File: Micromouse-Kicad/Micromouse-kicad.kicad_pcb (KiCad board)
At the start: 4 copper layers, 106.4 x 103.1 mm, 99 parts, among them J1 SWD, J2 USB_B_Micro, J3 UARTBTH, J4 Batería, J5 VL6180x, J6 MotorEncodL, J7 MotorEncodR, Q1 BS170, Q2 BS170, Q3 BS170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

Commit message: Cabra
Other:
- board text added: "RAS"

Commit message: Ajuste VL180X
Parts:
- moved J5 15.2 mm to (95.2, 110.5), turned to 180 degrees
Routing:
- net I2C2_SCL: track 72.0 -> 76.3 mm
- net I2C2_SDA: track 75.8 -> 77.2 mm, vias 3 -> 1
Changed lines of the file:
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@@
   )
   (footprint "Connector_PinSocket_2.54mm:PinSocket_1x07_P2.54mm_Vertical" (layer "F.Cu")
-    (at 95.275 95.27)
+    (at 95.25 110.49 180)
     (descr "Through hole straight socket strip, 1x07, 2.54mm pitch, single row (from Kicad 4.0.7), script generated")
     (tags "Through hole socket strip THT 1x07 2.54mm single row")
@@
     (fp_line (start -1.27 16.51) (end -1.27 -1.27) (layer "F.Fab") (width 0.1))
     (fp_line (start 0.635 -1.27) (end 1.27 -0.635) (layer "F.Fab") (width 0.1))
-    (pad "1" thru_hole rect (at 0 0) (size 1.7 1.7) (drill 1) (layers *.Cu *.Mask)
+    (pad "1" thru_hole rect (at 0 0 180) (size 1.7 1.7) (drill 1) (layers *.Cu *.Mask)
       (net 1 "+3.3V") (pinfunction "Pin_1") (pintype "passive"))
-    (pad "2" thru_hole oval (at 0 2.54) (size 1.7 1.7) (drill 1) (layers *.Cu *.Mask)
+    (pad "2" thru_hole oval (at 0 2.54 180) (size 1.7 1.7) (drill 1) (layers *.Cu *.Mask)
       (net 33 "unconnected-(J5-Pad2)") (pinfunction "Pin_2") (pintype "passive+no_connect"))
-    (pad "3" thru_hole oval (at 0 5.08) (size 1.7 1.7) (drill 1) (layers *.Cu *.Mask)
+    (pad "3" thru_hole oval (at 0 5.08 180) (size 1.7 1.7) (drill 1) (layers *.Cu *.Mask)
       (net 2 "GND") (pinfunction "Pin_3") (pintype "passive"))
-    (pad "4" thru_hole oval (at 0 7.62) (size 1.7 1.7) (drill 1) (layers *.Cu *.Mask)
+    (pad "4" thru_hole oval (at 0 7.62 180) (size 1.7 1.7) (drill 1) (layers *.Cu *.Mask)
       (net 34 "unconnected-(J5-Pad4)") (pinfunction "Pin_4") (pintype "passive+no_connect"))
-    (pad "5" thru_hole oval (at 0 10.16) (size 1.7 1.7) (drill 1) (layers *.Cu *.Mask)
+    (pad "5" thru_hole oval (at 0 10.16 180) (size 1.7 1.7) (drill 1) (layers *.Cu *.Mask)
       (net 35 "unconnected-(J5-Pad5)") (pinfunction "Pin_5") (pintype "passive+no_connect"))
-    (pad "6" thru_hole oval (at 0 12.7) (size 1.7 1.7) (drill 1) (layers *.Cu *.Mask)
+    (pad "6" thru_hole oval (at 0 12.7 180) (size 1.7 1.7) (drill 1) (layers *.Cu *.Mask)
       (net 36 "I2C2_SCL") (pinfunction "Pin_6") (pintype "passive"))
-    (pad "7" thru_hole oval (at 0 15.24) (size 1.7 1.7) (drill 1) (layers *.Cu *.Mask)
+    (pad "7" thru_hole oval (at 0 15.24 180) (size 1.7 1.7) (drill 1) (layers *.Cu *.Mask)
       (net 37 "I2C2_SDA") (pinfunction "Pin_7") (pintype "passive"))
     (model "${KICAD6_3DMODEL_DIR}/Connector_PinSocket_2.54mm.3dshapes/PinSocket_1x07_P2.54mm_Vertical.wrl"
@@
       (scale (xyz 1 1 1))
       (rotate (xyz 0 0 0))
+    )
+    (model "C:/Users/Tatan/3D Objects/KicadModels/vl6180x-carrier-model.step"
+      (offset (xyz 2.5 -16.25 12.8))
+      (scale (xyz 1 1 1))
+      (rotate (xyz 0 -90 0))
+    )
+    (model "C:/Users/Tatan/3D Objects/KicadModels/1x7 Male Pin Header Angle.STEP"
+      (offset (xyz 0 0.125 10))
+      (scale (xyz 1 1 1))
+      (rotate (xyz 90 0 -90))
     )
   )
@@
   (gr_line (start 128.778 128.016) (end 139.192 128.016) (layer "Edge.Cuts") (width 0.1))
   (gr_line (start 195.326 52.578) (end 195.326 152.654) (layer "Edge.Cuts") (width 0.1))
-  (gr_text "SDA" (at 98 110.85 90) (layer "F.SilkS")
+  (gr_text "SDA" (at 98.552 94.996 90) (layer "F.SilkS")
     (effects (font (size 1 1) (thickness 0.15)))
   )
@@
     (effects (font (size 1 1) (thickness 0.15)))
   )
-  (gr_text "SCL" (at 98.1 107.45 90) (layer "F.SilkS")
+  (gr_text "SCL" (at 98.552 98.044 90) (layer "F.SilkS")
     (effects (font (size 1 1) (thickness 0.15)))
   )
@@
     (effects (font (size 1 1) (thickness 0.15)))
   )
-  (gr_text "3.3v\n" (at 97.85 94.9 90) (layer "F.SilkS")
+  (gr_text "3.3v\n" (at 98.806 110.744 90) (layer "F.SilkS")
     (effects (font (size 1 1) (thickness 0.15)))
   )
-  (gr_text "GND\n" (at 97.9 100.05 90) (layer "F.SilkS")
+  (gr_text "GND\n" (at 98.806 105.41 90) (layer "F.SilkS")
     (effects (font (size 1 1) (thickness 0.15)))
   )
@@
   (via (at 146.7612 105.6781) (size 0.8) (drill 0.4) (layers "F.Cu" "B.Cu") (net 36))
   (via (at 148.0312 104.3291) (size 0.8) (drill 0.4) (layers "F.Cu" "B.Cu") (net 36))
+  (segment (start 95.25 97.79) (end 97.322733 97.79) (width 0.3) (layer "B.Cu") (net 36))
   (segment (start 142.727761 105.6781) (end 146.7612 105.6781) (width 0.3) (layer "B.Cu") (net 36))
   (segment (start 146.7612 105.6781) (end 148.0312 104.4081) (width 0.15) (layer "B.Cu") (net 36))
-  (segment (start 95.275 107.97) (end 140.435861 107.97) (width 0.3) (layer "B.Cu") (net 36))
   (segment (start 148.0312 104.4081) (end 148.0312 104.3291) (width 0.15) (layer "B.Cu") (net 36))
   (segment (start 140.435861 107.97) (end 142.727761 105.6781) (width 0.3) (layer "B.Cu") (net 36))
+  (segment (start 97.322733 97.79) (end 107.502733 107.97) (width 0.3) (layer "B.Cu") (net 36))
+  (segment (start 107.502733 107.97) (end 140.435861 107.97) (width 0.3) (layer "B.Cu") (net 36))
   (segment (start 157.1264 105.0036) (end 157.8376 105.7148) (width 0.15) (layer "F.Cu") (net 37))
   (segment (start 144.0826 105.0036) (end 149.9964 105.0036) (width 0.15) (layer "F.Cu") (net 37))
@@
   (segment (start 149.9964 105.0036) (end 157.1264 105.0036) (width 0.15) (layer "F.Cu") (net 37))
   (segment (start 157.9324 105.62) (end 159.35 105.62) (width 0.3) (layer "F.Cu") (net 37))
-  (segment (start 114.15 109.1) (end 114.15 107.5) (width 0.3) (layer "F.Cu") (net 37))
   (segment (start 139.75 106.9) (end 148.1 106.9) (width 0.3) (layer "F.Cu") (net 37))
   (segment (start 157.8376 105.7148) (end 157.9324 105.62) (width 0.3) (layer "F.Cu") (net 37))
-  (segment (start 114.15 107.5) (end 116.05 105.6) (width 0.3) (layer "F.Cu") (net 37))
   (segment (start 148.1 106.9) (end 149.9964 105.0036) (width 0.3) (layer "F.Cu") (net 37))
   (via (at 139.75 106.9) (size 0.55) (drill 0.4) (layers "F.Cu" "B.Cu") (net 37))
-  (via (at 116.05 105.6) (size 0.55) (drill 0.4) (layers "F.Cu" "B.Cu") (net 37))
-  (via (at 114.15 109.1) (size 0.55) (drill 0.4) (layers "F.Cu" "B.Cu") (net 37))
   (segment (start 138.45 105.6) (end 139.75 106.9) (width 0.3) (layer "B.Cu") (net 37))
+  (segment (start 105.7 95.25) (end 95.25 95.25) (width 0.3) (layer "B.Cu") (net 37))
   (segment (start 116.05 105.6) (end 138.45 105.6) (width 0.3) (layer "B.Cu") (net 37))
-  (segment (start 95.275 110.51) (end 96.685 109.1) (width 0.3) (layer "B.Cu") (net 37))
-  (segment (start 96.685 109.1) (end 114.15 109.1) (width 0.3) (layer "B.Cu") (net 37))
+  (segment (start 116.05 105.6) (end 105.7 95.25) (width 0.3) (layer "B.Cu") (net 37))
   (segment (start 174.8536 104.5464) (end 174.8536 104.902) (width 0.261112) (layer "F.Cu") (net 38))
   (segment (start 182.178 97.222) (end 174.8536 104.5464) (width 0.261112) (layer "F.Cu") (net 38))

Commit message: arreglo módulo frontal
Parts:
- moved J5 15.9 mm to (100.3, 95.4), turned to 0 degrees
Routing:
- net I2C2_SCL: track 76.3 -> 67.0 mm
- net I2C2_SDA: track 77.2 -> 69.2 mm
- net L_Reciever: track 83.5 -> 82.2 mm
- net /HSE_IN: track 7.44 -> 6.62 mm
- net GND: track 138.1 -> 137.4 mm
- net Net-(R18-Pad1): track 2.24 -> 1.63 mm
- net Net-(R9-Pad1): track 2.31 -> 1.71 mm
- net Net-(R17-Pad1): track 2.11 -> 1.55 mm
- net +3.3V: track 90.2 -> 89.7 mm
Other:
- board size 106.4 x 103.1 mm -> 99.2 x 98.9 mm
- board text removed: "3.3v"
- board text removed: "SCL"
- board text removed: "SDA"

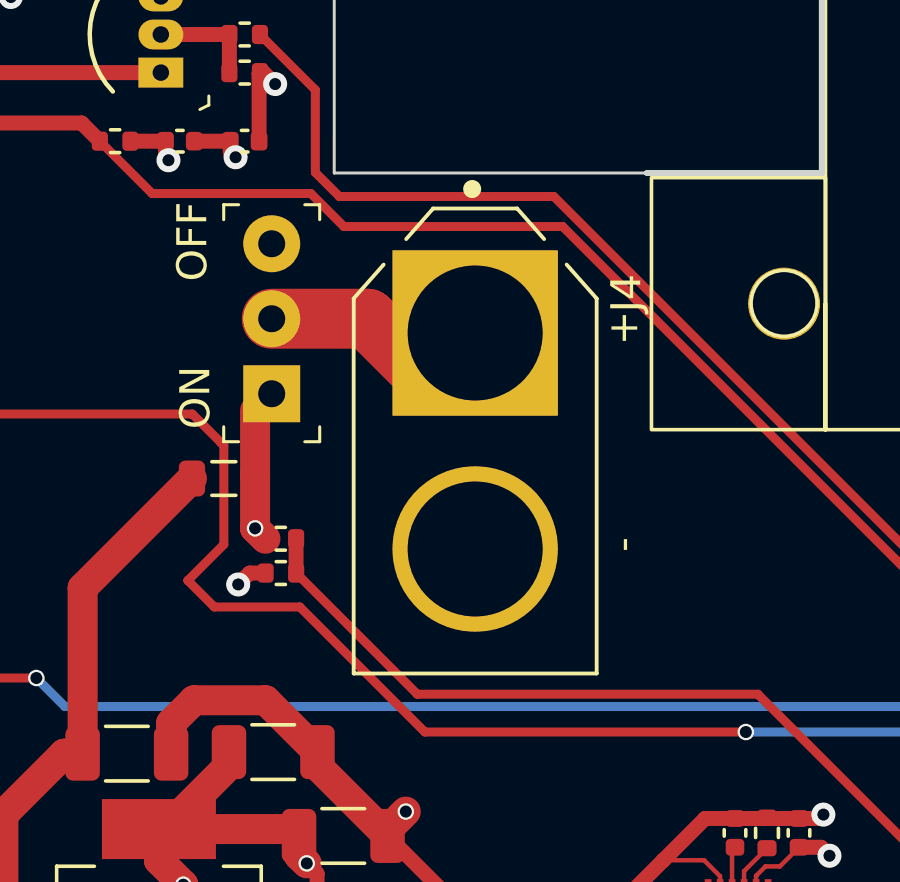
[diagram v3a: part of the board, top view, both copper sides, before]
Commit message: arreglo conector potencia
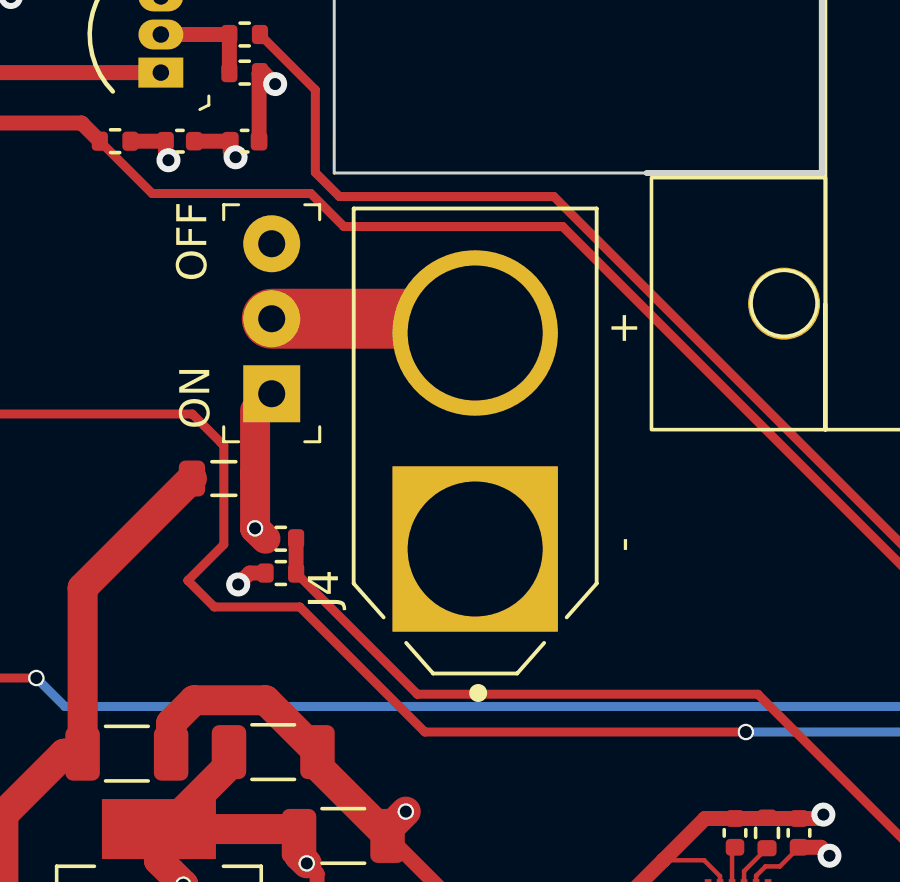
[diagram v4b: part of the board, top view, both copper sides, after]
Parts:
- turned J4 to 90 degrees
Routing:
- net VAA: track 6.07 -> 6.98 mm

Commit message: Arreglos pines stm32
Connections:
- J3 pad 4: UART4_RX -> USART2_RX
- J3 pad 5: UART4_TX -> USART2_TX
- J4 pad 1: GND -> VAA
- J4 pad 2: VAA -> GND
- RU1 pad 2: /USB_STM32_D+ -> DP
- RU2 pad 2: /USB_STM32_D- -> DM
- RU3 pad 2: /USB_STM32_D+ -> DP
- U1 pad 16: FR_Emitter -> USART2_TX
- U1 pad 17: FL_Emitter -> USART2_RX
- U1 pad 20: R_Emitter -> unconnected-(U1-PA4-Pad20)
- U1 pad 21: L_Emitter -> R_Emitter
- U1 pad 22: unconnected-(U1-Pad22) -> L_Emitter
- U1 pad 23: unconnected-(U1-Pad23) -> FR_Emitter
- U1 pad 26: unconnected-(U1-Pad26) -> FL_Emitter
- U1 pad 35: UART4_TX -> DM
- U1 pad 36: UART4_RX -> DP
- U1 pad 52: /USB_STM32_D- -> unconnected-(U1-PC11-Pad52)
- U1 pad 53: /USB_STM32_D+ -> unconnected-(U1-PC12-Pad53)
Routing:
- net (no net): track 0.00 -> 140.3 mm, vias 0 -> 1
- net UART4_RX: track 54.9 -> 0.00 mm, vias 1 -> 0
- net UART4_TX: track 49.9 -> 0.00 mm
- net /USB_STM32_D+: track 18.6 -> 0.00 mm
- net /USB_STM32_D-: track 16.8 -> 0.00 mm

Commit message: Fabricado!
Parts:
- added ?: , , F.Cu at (186.7, 61.8)
- added ?: , , F.Cu at (186.7, 144.7)
- added ?: , , F.Cu at (109.6, 99.8)
- J6, J7: footprint Connector_JST:JST_XH_B6B-XH-A_1x06_P2.50mm_Vertical -> Connector_JST:JST_SH_BM06B-SRSS-TB_1x06-1MP_P1.00mm_Vertical
- moved J5 15.2 mm to (100.3, 110.6), turned to 180 degrees
- moved RU1 13.2 mm to (163.6, 113.2), turned to 90 degrees
- moved J6 6.49 mm to (186.0, 90.4)
- moved J7 6.48 mm to (186.0, 72.2)
- moved DL2 1.67 mm to (166.4, 116.4), turned to 180 degrees
- moved R1 1.11 mm to (165.6, 113.9)
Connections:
- net DM renamed /USB_STM32_D-
- net DP renamed /USB_STM32_D+
- J4 pad 1: VAA -> GND
- J4 pad 2: GND -> VAA
- U1 pad 21: R_Emitter -> L_Emitter
- U1 pad 22: L_Emitter -> R_Emitter
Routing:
- net (no net): track 140.3 -> 0.00 mm, vias 1 -> 0
- net USART2_RX: track 0.00 -> 51.2 mm, vias 0 -> 2
- net /USB_STM32_D+: track 0.00 -> 41.8 mm, vias 0 -> 4
- net /USB_STM32_D-: track 0.00 -> 41.3 mm, vias 0 -> 4
- net USART2_TX: track 0.00 -> 41.3 mm, vias 0 -> 2
- net +3.3V: track 89.7 -> 94.8 mm, vias 27 -> 31
- net OutML1: track 6.98 -> 12.0 mm
- net TIM8_CH1: track 40.4 -> 35.5 mm
- net FR_Emitter: track 63.5 -> 59.4 mm
- net I2C2_SDA: track 69.2 -> 72.6 mm
- net GND: track 137.4 -> 140.5 mm, vias 48 -> 52
- net TIM1_CH2: track 42.5 -> 45.5 mm
- net RST: track 46.9 -> 43.8 mm
- net I2C2_SCL: track 67.0 -> 69.5 mm
- net OutML2: track 19.1 -> 21.3 mm
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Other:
- board text added: "JSOR"
- board text added: "t4dzi0"
